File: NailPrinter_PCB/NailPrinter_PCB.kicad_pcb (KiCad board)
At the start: 2 copper layers, 233.5 x 103 mm, 37 parts, among them J1 Barrel_Jack, J10 Conn_01x24, J2 Conn_01x03, J3 Conn_01x04, J4 Conn_01x04, J5 Conn_01x04, J6 Conn_01x04, J7 Conn_01x03, J8 Conn_01x04, J9 Conn_01x24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

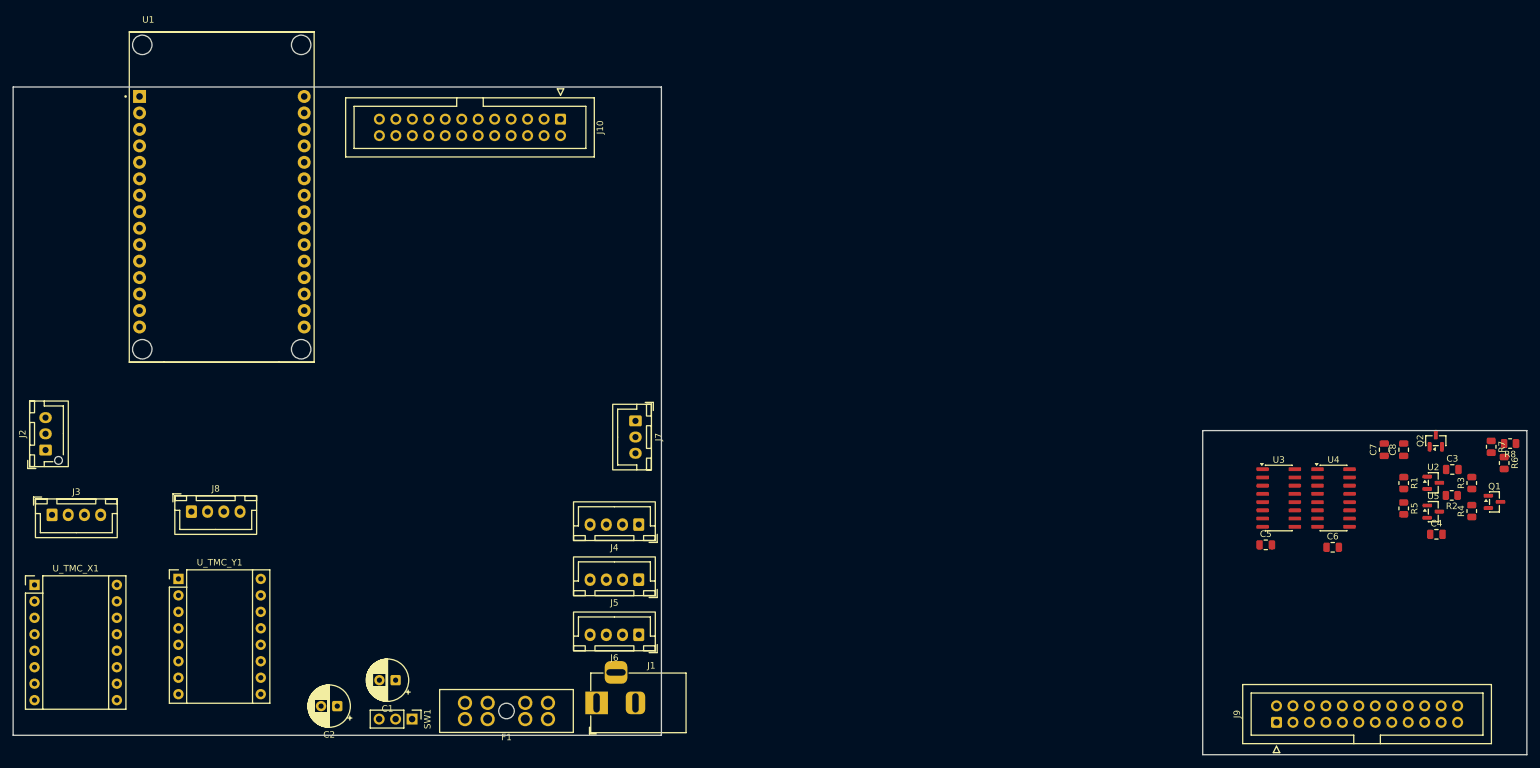
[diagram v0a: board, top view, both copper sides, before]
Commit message: Placed components on pcb
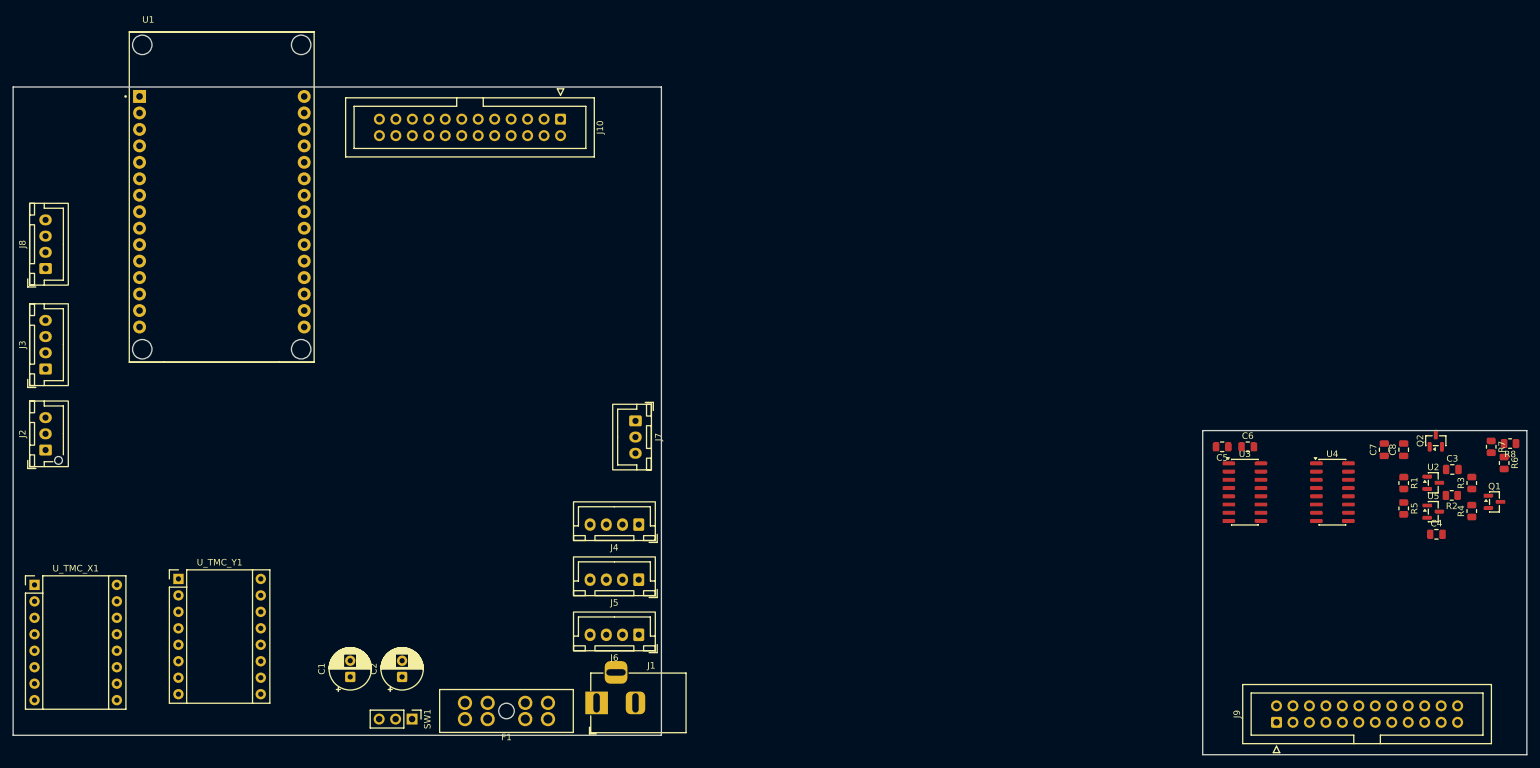
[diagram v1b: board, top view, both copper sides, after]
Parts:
- moved J8 43.7 mm to (20.0, 64.5), turned to 90 degrees
- moved J3 22.5 mm to (20.0, 80.0), turned to 90 degrees
- moved C6 20.3 mm to (205.4, 92.0)
- moved C5 16.6 mm to (201.5, 92.0), turned to 180 degrees
- moved C2 11.0 mm to (75.0, 127.5), turned to 90 degrees
- moved C1 7.02 mm to (67.0, 127.5), turned to 90 degrees
- moved U3 5.30 mm to (205.0, 99.0)
- moved U4 0.92 mm to (218.5, 99.0)

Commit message: Added TODO list to readme. Routed Mainboard PCB
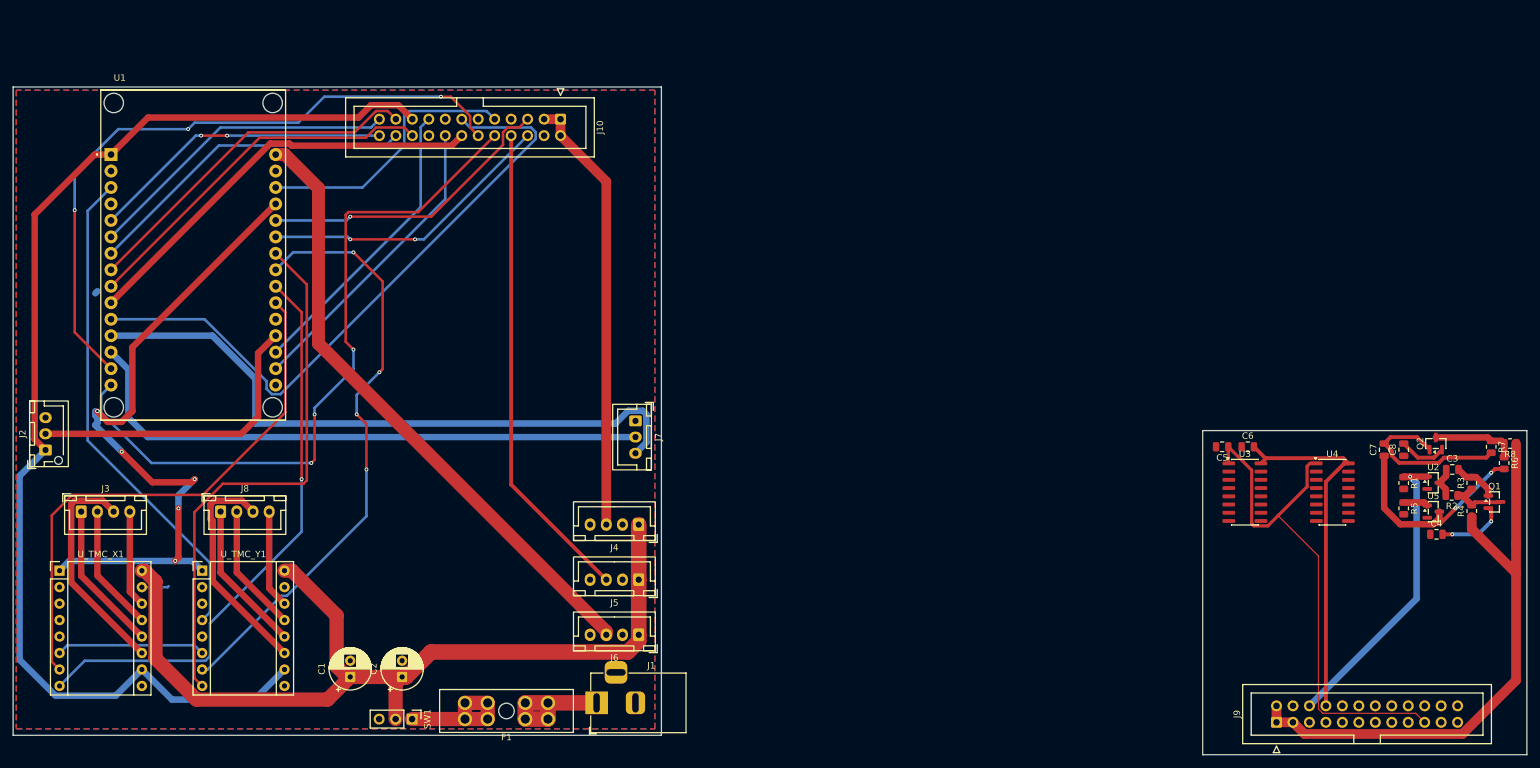
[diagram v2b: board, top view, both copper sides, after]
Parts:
- moved J8 46.2 mm to (47.0, 102.0), turned to 0 degrees
- moved J3 22.7 mm to (25.5, 102.0), turned to 0 degrees
- moved U1 9.98 mm to (42.8, 62.4)
- moved U_TMC_X1 4.44 mm to (22.2, 111.1)
- moved U_TMC_Y1 3.87 mm to (44.2, 111.1)
- moved Q2 0.44 mm to (234.4, 91.5)
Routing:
- net +3.3V: track 0.00 -> 267.4 mm
- net +16V: track 0.00 -> 159.7 mm
- net +24V: track 0.00 -> 142.0 mm
- net +9V: track 0.00 -> 130.6 mm
- net CLK_3V: track 0.00 -> 110.0 mm, vias 0 -> 3
- net EN_MOTORS: track 0.00 -> 107.0 mm, vias 0 -> 6
- net D1_3V: track 0.00 -> 103.2 mm, vias 0 -> 3
- net D2_3V: track 0.00 -> 100.6 mm
- net Net-(J7-Pin_3): track 0.00 -> 100.0 mm
- net +5V: track 0.00 -> 96.0 mm
- net STEP_Y: track 0.00 -> 93.1 mm, vias 0 -> 4
- net PWRA_IN: track 0.00 -> 91.9 mm, vias 0 -> 3
- net Net-(J7-Pin_2): track 0.00 -> 90.7 mm
- net DIR_X: track 0.00 -> 89.7 mm, vias 0 -> 1
- net STEP_X: track 0.00 -> 84.4 mm
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- added copper zone on B.Cu, net GND
- added copper zone on F.Cu, net GND

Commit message: Adjusting traces for the sake of signal integrity
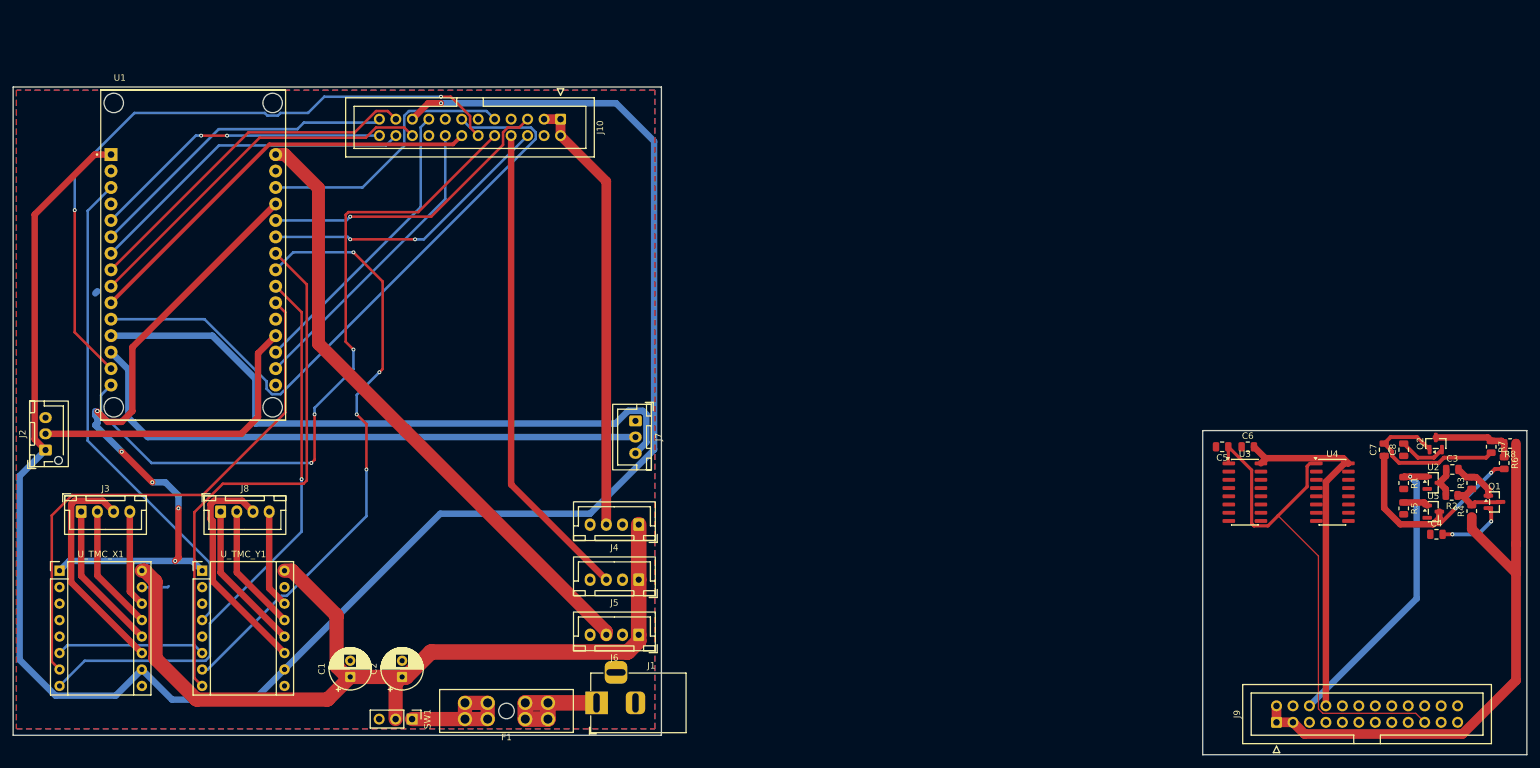
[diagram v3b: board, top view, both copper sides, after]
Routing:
- net +3.3V: track 267.4 -> 376.2 mm, vias 0 -> 1
- net EN_MOTORS: track 107.0 -> 101.6 mm
- net D1_3V: track 103.2 -> 103.5 mm, vias 3 -> 2
